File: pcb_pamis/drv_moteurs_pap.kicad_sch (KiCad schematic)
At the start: 13 parts, among them J4 Conn_01x04, J5 Conn_01x04, J6 Conn_01x04, U3 TMC2209_SILENTSTEPSTICK, U4 TMC2209_SILENTSTEPSTICK, U5 TMC2209_SILENTSTEPSTICK

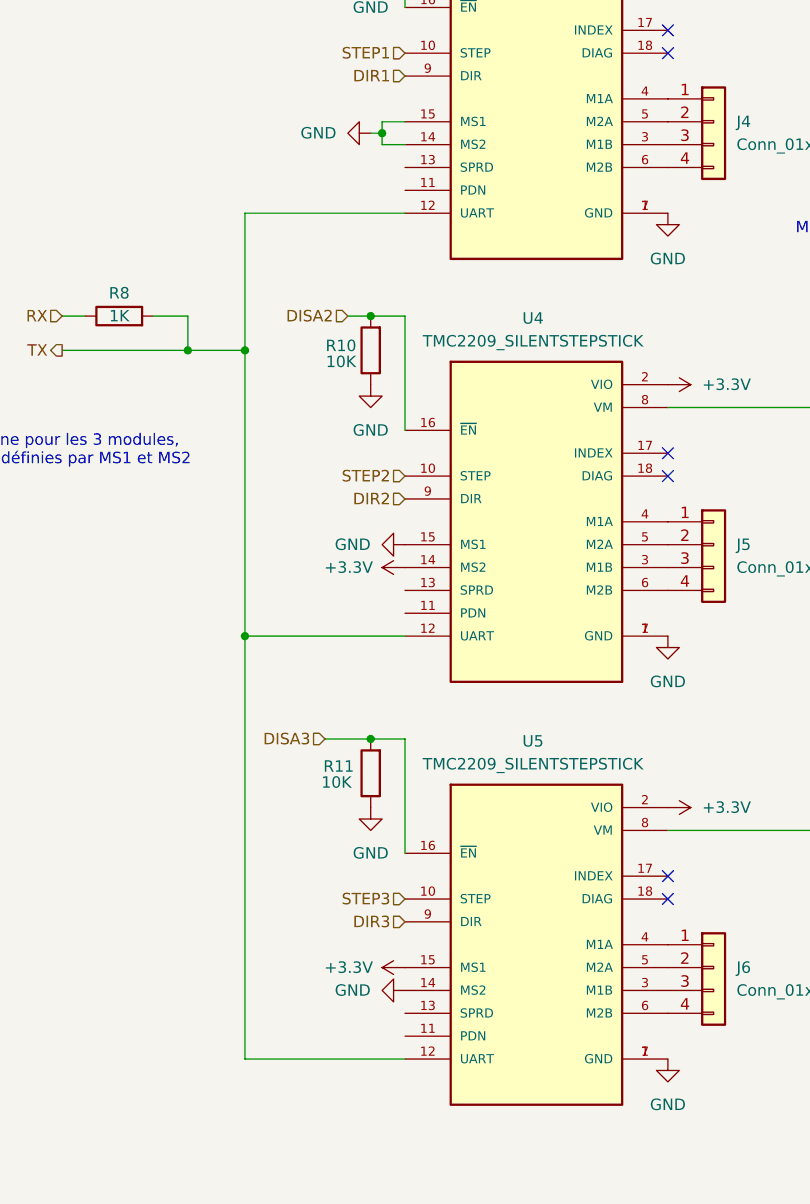
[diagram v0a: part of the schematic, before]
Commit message: ajout d'un connecteur pour les GPIO restant
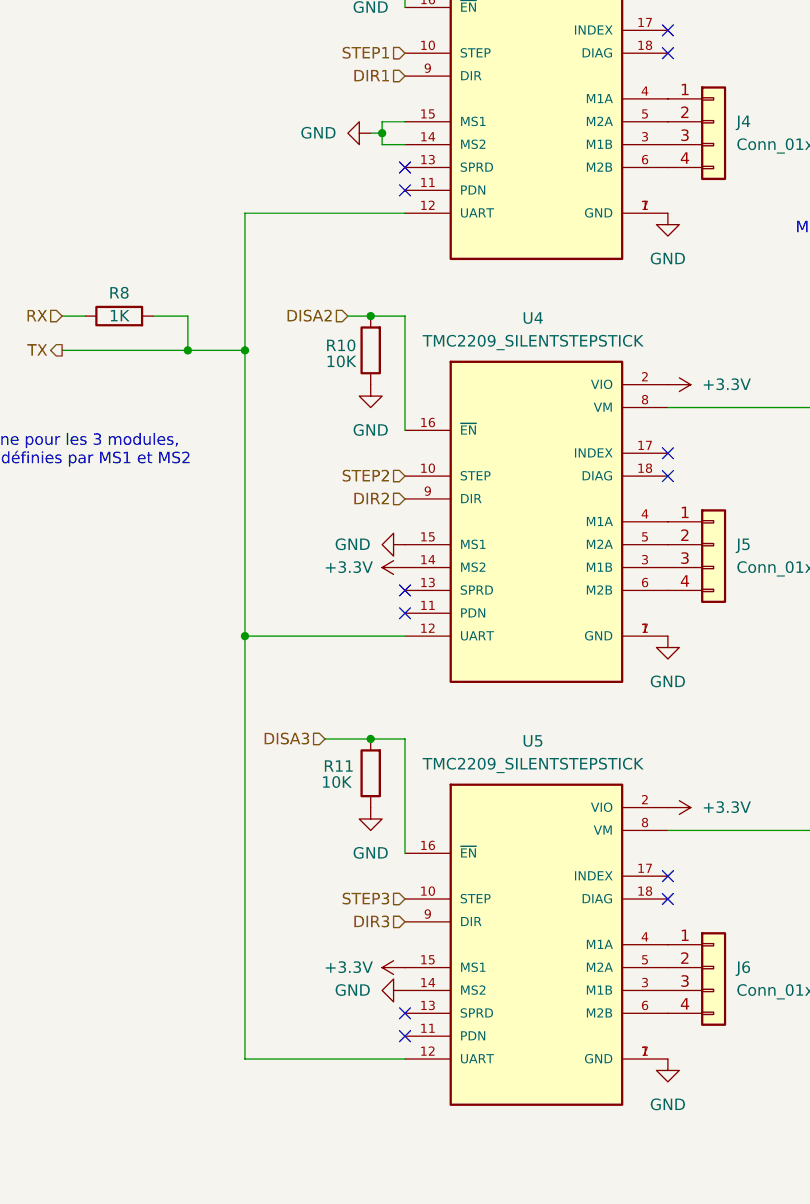
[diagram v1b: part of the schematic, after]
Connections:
- no-connect marks 6 -> 12
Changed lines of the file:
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@@
+	)
+	(no_connect
+		(at 91.44 63.5)
+	)
+	(no_connect
+		(at 91.44 110.49)
 	)
 	(no_connect
@@
 	)
 	(no_connect
+		(at 91.44 60.96)
+	)
+	(no_connect
 		(at 120.65 139.7)
+	)
+	(no_connect
+		(at 91.44 107.95)
 	)
 	(no_connect
@@
 	)
 	(no_connect
+		(at 91.44 157.48)
+	)
+	(no_connect
 		(at 120.65 142.24)
 	)
+	(no_connect
+		(at 91.44 154.94)
+	)
 	(wire

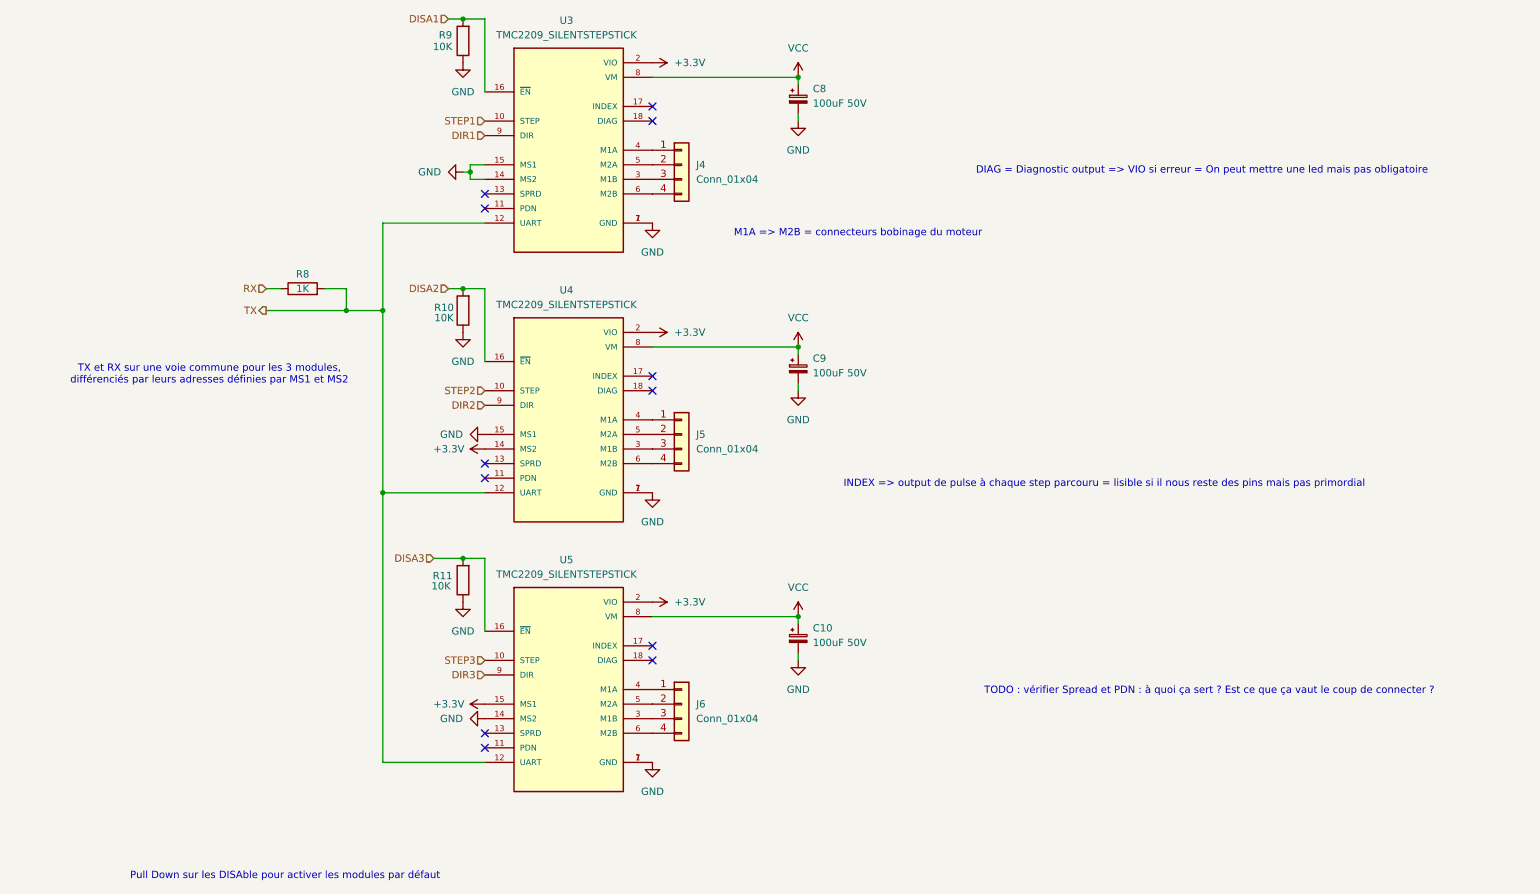
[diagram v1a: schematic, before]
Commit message: Ajout connecteurs, diodes sur arrêt moteurs et finalisation du schéma
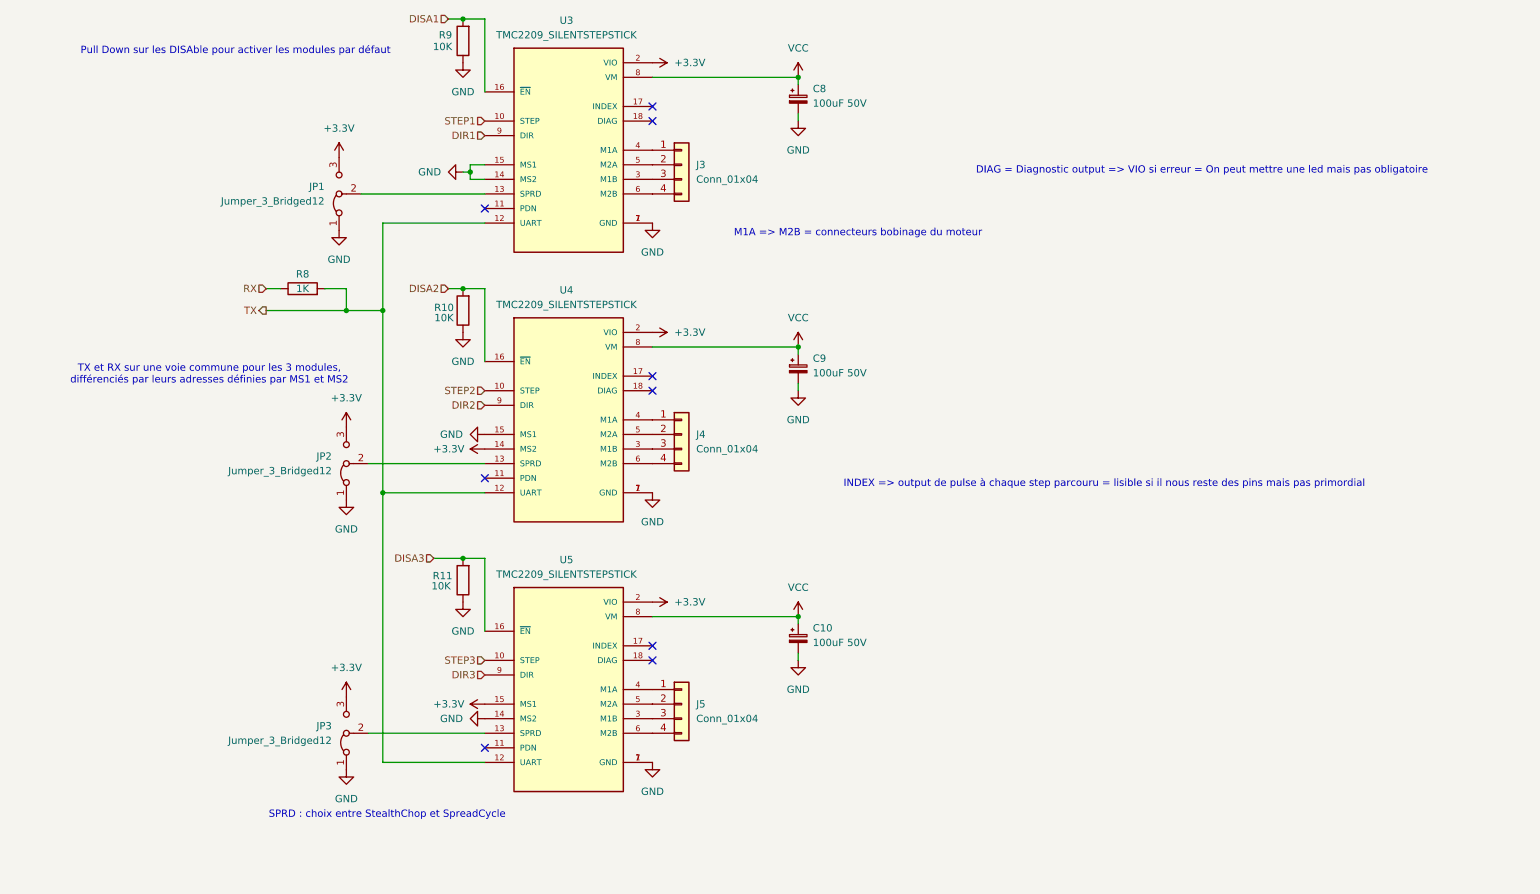
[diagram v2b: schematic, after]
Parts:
- added JP1, JP2, JP3: Jumper_3_Bridged12, symbol Jumper:Jumper_3_Bridged12
- renumbered J4 to J3, J5 to J4, J6 to J5
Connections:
- net +3.3V: now also JP1.3 (B), JP2.3 (B), JP3.3 (B)
- net GND: now also JP1.1 (A), JP2.1 (A), JP3.1 (A)
- net at U5.13 (SPRD): now also JP3.2 (C)
- net at U4.13 (SPRD): now also JP2.2 (C)
- net at U3.13 (SPRD): now also JP1.2 (C)
- no-connect marks 12 -> 9
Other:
- note added: "SPRD : choix entre StealthChop et SpreadCycle"
- note removed: "TODO : vérifier Spread et PDN : à quoi ça sert ? Est ce que ça vaut le coup de connecter ?"

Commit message: ajout des empreintes pour le pcb PAMI
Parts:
- C10, C8, C9: footprint (none) -> Capacitor_SMD:C_0805_2012Metric_Pad1.18x1.45mm_HandSolder
- J3, J4, J5: footprint (none) -> Connector_PinHeader_1.27mm:PinHeader_1x04_P1.27mm_Vertical
- JP1, JP2, JP3: footprint (none) -> Connector_PinHeader_1.27mm:PinHeader_1x02_P1.27mm_Vertical
- R10, R11, R8, R9: footprint (none) -> Resistor_SMD:R_0805_2012Metric_Pad1.20x1.40mm_HandSolder
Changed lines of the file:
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@@
 			)
 		)
-		(property "Footprint" ""
+		(property "Footprint" "Resistor_SMD:R_0805_2012Metric_Pad1.20x1.40mm_HandSolder"
 			(at 59.69 79.248 90)
 			(effects
@@
 			)
 		)
-		(property "Footprint" ""
+		(property "Footprint" "Connector_PinHeader_1.27mm:PinHeader_1x02_P1.27mm_Vertical"
 			(at 67.31 107.95 0)
 			(effects
@@
 			)
 		)
-		(property "Footprint" ""
+		(property "Footprint" "Resistor_SMD:R_0805_2012Metric_Pad1.20x1.40mm_HandSolder"
 			(at 89.408 34.29 90)
 			(effects
@@
 			)
 		)
-		(property "Footprint" ""
+		(property "Footprint" "Connector_PinHeader_1.27mm:PinHeader_1x02_P1.27mm_Vertical"
 			(at 67.31 154.94 0)
 			(effects
@@
 			)
 		)
-		(property "Footprint" ""
+		(property "Footprint" "Capacitor_SMD:C_0805_2012Metric_Pad1.18x1.45mm_HandSolder"
 			(at 146.05 138.43 0)
 			(effects
@@
 			)
 		)
-		(property "Footprint" ""
+		(property "Footprint" "Connector_PinHeader_1.27mm:PinHeader_1x04_P1.27mm_Vertical"
 			(at 125.73 149.86 0)
 			(effects
@@
 			)
 		)
-		(property "Footprint" ""
+		(property "Footprint" "Resistor_SMD:R_0805_2012Metric_Pad1.20x1.40mm_HandSolder"
 			(at 89.408 128.27 90)
 			(effects
@@
 			)
 		)
-		(property "Footprint" ""
+		(property "Footprint" "Capacitor_SMD:C_0805_2012Metric_Pad1.18x1.45mm_HandSolder"
 			(at 146.05 44.45 0)
 			(effects
@@
 			)
 		)
-		(property "Footprint" ""
+		(property "Footprint" "Connector_PinHeader_1.27mm:PinHeader_1x04_P1.27mm_Vertical"
 			(at 125.73 55.88 0)
 			(effects
@@
 			)
 		)
-		(property "Footprint" ""
+		(property "Footprint" "Connector_PinHeader_1.27mm:PinHeader_1x04_P1.27mm_Vertical"
 			(at 125.73 102.87 0)
 			(effects
@@
 			)
 		)
-		(property "Footprint" ""
+		(property "Footprint" "Connector_PinHeader_1.27mm:PinHeader_1x02_P1.27mm_Vertical"
 			(at 66.04 60.96 0)
 			(effects
@@
 			)
 		)
-		(property "Footprint" ""
+		(property "Footprint" "Capacitor_SMD:C_0805_2012Metric_Pad1.18x1.45mm_HandSolder"
 			(at 146.05 91.44 0)
 			(effects
@@
 			)
 		)
-		(property "Footprint" ""
+		(property "Footprint" "Resistor_SMD:R_0805_2012Metric_Pad1.20x1.40mm_HandSolder"
 			(at 89.408 81.28 90)
 			(effects

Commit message: finalisation empreintes des composants
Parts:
- C10, C8, C9: footprint Capacitor_SMD:C_0805_2012Metric_Pad1.18x1.45mm_HandSolder -> Capacitor_THT:CP_Radial_D8.0mm_P3.80mm
- JP1, JP2, JP3: footprint Connector_PinHeader_1.27mm:PinHeader_1x02_P1.27mm_Vertical -> Connector_PinHeader_1.27mm:PinHeader_1x03_P1.27mm_Vertical
- U3, U4, U5: footprint TMC2209_SILENTSTEPSTICK:MODULE_TMC2209_SILENTSTEPSTICK -> Modelec:MODULE_TMC2209_SILENTSTEPSTICK
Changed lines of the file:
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@@
 			)
 		)
-		(property "Footprint" "TMC2209_SILENTSTEPSTICK:MODULE_TMC2209_SILENTSTEPSTICK"
+		(property "Footprint" "Modelec:MODULE_TMC2209_SILENTSTEPSTICK"
 			(at 104.14 147.32 0)
 			(effects
@@
 			)
 		)
-		(property "Footprint" "Connector_PinHeader_1.27mm:PinHeader_1x02_P1.27mm_Vertical"
+		(property "Footprint" "Connector_PinHeader_1.27mm:PinHeader_1x03_P1.27mm_Vertical"
 			(at 67.31 107.95 0)
 			(effects
@@
 			)
 		)
-		(property "Footprint" "TMC2209_SILENTSTEPSTICK:MODULE_TMC2209_SILENTSTEPSTICK"
+		(property "Footprint" "Modelec:MODULE_TMC2209_SILENTSTEPSTICK"
 			(at 104.14 100.33 0)
 			(effects
@@
 			)
 		)
-		(property "Footprint" "TMC2209_SILENTSTEPSTICK:MODULE_TMC2209_SILENTSTEPSTICK"
+		(property "Footprint" "Modelec:MODULE_TMC2209_SILENTSTEPSTICK"
 			(at 104.14 53.34 0)
 			(effects
@@
 			)
 		)
-		(property "Footprint" "Connector_PinHeader_1.27mm:PinHeader_1x02_P1.27mm_Vertical"
+		(property "Footprint" "Connector_PinHeader_1.27mm:PinHeader_1x03_P1.27mm_Vertical"
 			(at 67.31 154.94 0)
 			(effects
@@
 			)
 		)
-		(property "Footprint" "Capacitor_SMD:C_0805_2012Metric_Pad1.18x1.45mm_HandSolder"
+		(property "Footprint" "Capacitor_THT:CP_Radial_D8.0mm_P3.80mm"
 			(at 146.05 138.43 0)
 			(effects
@@
 			)
 		)
-		(property "Footprint" "Capacitor_SMD:C_0805_2012Metric_Pad1.18x1.45mm_HandSolder"
+		(property "Footprint" "Capacitor_THT:CP_Radial_D8.0mm_P3.80mm"
 			(at 146.05 44.45 0)
 			(effects
@@
 			)
 		)
-		(property "Footprint" "Connector_PinHeader_1.27mm:PinHeader_1x02_P1.27mm_Vertical"
+		(property "Footprint" "Connector_PinHeader_1.27mm:PinHeader_1x03_P1.27mm_Vertical"
 			(at 66.04 60.96 0)
 			(effects
@@
 			)
 		)
-		(property "Footprint" "Capacitor_SMD:C_0805_2012Metric_Pad1.18x1.45mm_HandSolder"
+		(property "Footprint" "Capacitor_THT:CP_Radial_D8.0mm_P3.80mm"
 			(at 146.05 91.44 0)
 			(effects

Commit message: commencement correctifs PCB Pami
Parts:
- J3, J4, J5: footprint Connector_PinHeader_1.27mm:PinHeader_1x04_P1.27mm_Vertical -> Connector_PinHeader_2.54mm:PinHeader_1x04_P2.54mm_Vertical
- JP1, JP2, JP3: footprint Connector_PinHeader_1.27mm:PinHeader_1x03_P1.27mm_Vertical -> Connector_PinHeader_2.54mm:PinHeader_1x03_P2.54mm_Vertical
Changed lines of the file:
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@@
 			)
 		)
-		(property "Footprint" "Connector_PinHeader_1.27mm:PinHeader_1x03_P1.27mm_Vertical"
+		(property "Footprint" "Connector_PinHeader_2.54mm:PinHeader_1x03_P2.54mm_Vertical"
 			(at 67.31 107.95 0)
 			(effects
@@
 			)
 		)
-		(property "Footprint" "Connector_PinHeader_1.27mm:PinHeader_1x03_P1.27mm_Vertical"
+		(property "Footprint" "Connector_PinHeader_2.54mm:PinHeader_1x03_P2.54mm_Vertical"
 			(at 67.31 154.94 0)
 			(effects
@@
 			)
 		)
-		(property "Footprint" "Connector_PinHeader_1.27mm:PinHeader_1x04_P1.27mm_Vertical"
+		(property "Footprint" "Connector_PinHeader_2.54mm:PinHeader_1x04_P2.54mm_Vertical"
 			(at 125.73 149.86 0)
 			(effects
@@
 			)
 		)
-		(property "Footprint" "Connector_PinHeader_1.27mm:PinHeader_1x04_P1.27mm_Vertical"
+		(property "Footprint" "Connector_PinHeader_2.54mm:PinHeader_1x04_P2.54mm_Vertical"
 			(at 125.73 55.88 0)
 			(effects
@@
 			)
 		)
-		(property "Footprint" "Connector_PinHeader_1.27mm:PinHeader_1x04_P1.27mm_Vertical"
+		(property "Footprint" "Connector_PinHeader_2.54mm:PinHeader_1x04_P2.54mm_Vertical"
 			(at 125.73 102.87 0)
 			(effects
@@
 			)
 		)
-		(property "Footprint" "Connector_PinHeader_1.27mm:PinHeader_1x03_P1.27mm_Vertical"
+		(property "Footprint" "Connector_PinHeader_2.54mm:PinHeader_1x03_P2.54mm_Vertical"
 			(at 66.04 60.96 0)
 			(effects

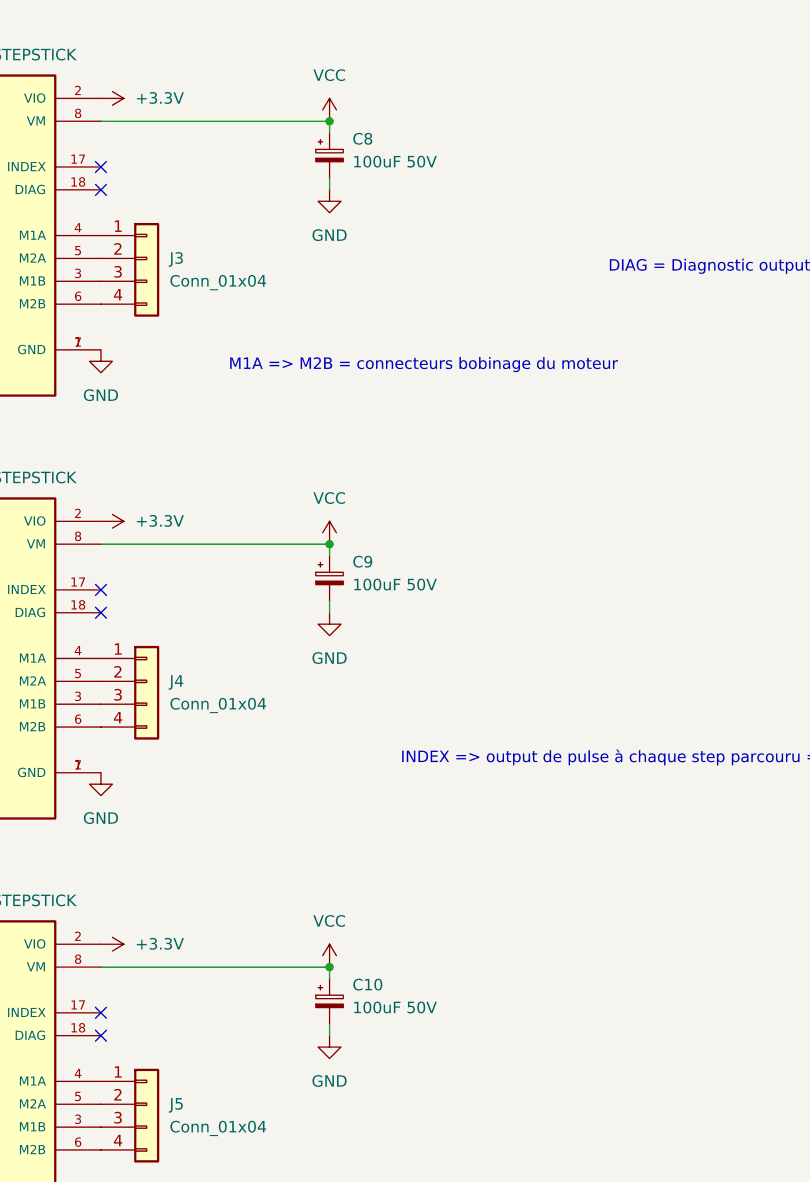
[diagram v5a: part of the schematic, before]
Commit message: finalisation nouveau routage
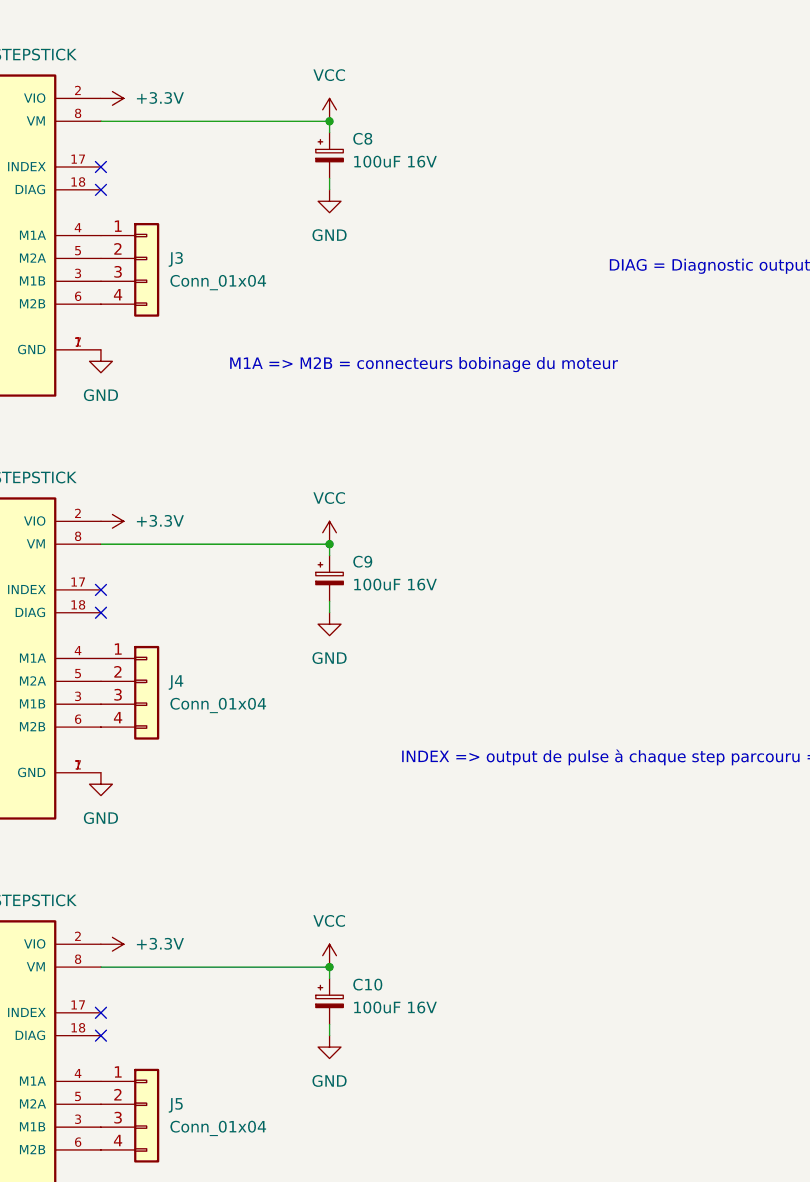
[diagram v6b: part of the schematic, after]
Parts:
- C10, C8, C9: value 100uF 50V -> 100uF 16V; footprint Capacitor_THT:CP_Radial_D8.0mm_P3.80mm -> Capacitor_THT:CP_Radial_D5.0mm_P2.00mm
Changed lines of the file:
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@@
 			)
 		)
-		(property "Value" "100uF 50V"
+		(property "Value" "100uF 16V"
 			(at 148.59 139.1538 0)
 			(effects
@@
 			)
 		)
-		(property "Footprint" "Capacitor_THT:CP_Radial_D8.0mm_P3.80mm"
+		(property "Footprint" "Capacitor_THT:CP_Radial_D5.0mm_P2.00mm"
 			(at 146.05 138.43 0)
 			(effects
@@
 			)
 		)
-		(property "Value" "100uF 50V"
+		(property "Value" "100uF 16V"
 			(at 148.59 45.1738 0)
 			(effects
@@
 			)
 		)
-		(property "Footprint" "Capacitor_THT:CP_Radial_D8.0mm_P3.80mm"
+		(property "Footprint" "Capacitor_THT:CP_Radial_D5.0mm_P2.00mm"
 			(at 146.05 44.45 0)
 			(effects
@@
 			)
 		)
-		(property "Value" "100uF 50V"
+		(property "Value" "100uF 16V"
 			(at 148.59 92.1638 0)
 			(effects
@@
 			)
 		)
-		(property "Footprint" "Capacitor_THT:CP_Radial_D8.0mm_P3.80mm"
+		(property "Footprint" "Capacitor_THT:CP_Radial_D5.0mm_P2.00mm"
 			(at 146.05 91.44 0)
 			(effects
